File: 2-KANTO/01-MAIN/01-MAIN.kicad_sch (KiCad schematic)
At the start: 69 parts, among them J1 WRITER CONN, J2 Conn_01x05, J3 STS3032, J4 STS3032, J5 STS3032, J6 STS3032, J7 LOADCELL_R, J8 LOADCELL_L, Q1 2SA1015, U1 STM32F446RETx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

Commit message: mike
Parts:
- removed D2, D3, D4, D5, D6, D7, D8, D9: WS2812B, LED_SMD:LED_WS2812B_PLCC4_5.0x5.0mm_P3.2mm, symbol LED:WS2812B
- removed RV1, RV2, RV3: R_Trim, Potentiometer_THT:Potentiometer_Bourns_3296W_Vertical, symbol Device:R_Potentiometer_Trim_US
- added H1: ToMainVDD, MountingHole:MountingHole_3.2mm_M3_Pad_Via, symbol Mechanical:MountingHole_Pad
- added H2: ToMainGND, MountingHole:MountingHole_3.2mm_M3_Pad_Via, symbol Mechanical:MountingHole_Pad
- added J9: MAIN Conn, Connector_JST:JST_XH_B8B-XH-A_1x08_P2.50mm_Vertical, symbol Connector_Generic:Conn_01x08
- added R21, R22: 2.2k, Resistor_SMD:R_0603_1608Metric, symbol Device:R
- added R23: 1.5k, Resistor_SMD:R_0603_1608Metric, symbol Device:R
- J1: footprint Connector_PinSocket_2.54mm:PinSocket_2x04_P2.54mm_Vertical -> Connector_PinSocket_2.54mm:PinSocket_2x04_P2.54mm_Horizontal
- J2: value Conn_01x05 -> toLINE
- J3, J4, J5, J6: footprint Connector_JST:JST_XH_B3B-XH-A_1x03_P2.50mm_Vertical -> Connector_Molex:Molex_SPOX_5267-03A_1x03_P2.50mm_Vertical
- R12, R13, R14, R15: value 330k -> 1M; LCSC C23137 -> C22935
- R16, R17, R18, R19: LCSC C137819 -> C25804
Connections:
- net CK1 is gone; now on net Battery_obs: U1.62 (PB9)
- net Dout1 is gone; now on net I2C1_SDA: U1.59 (PB7)
- net Range1 is gone; now on net I2C2_SCL: U1.29 (PB10)
- net photo_L_6 is gone; now on net LOADCEL_L: U1.9 (PC1)
- net photo_L_7 is gone; now on net LOADCEL_R: U1.8 (PC0)
- net photo_R_1 is gone; now on net XSHUT1: U1.21 (PA5)
- net photo_R_2 is gone; now on net XSHUT2: U1.22 (PA6)
- net photo_R_3 is gone; now on net XSHUT3: U1.23 (PA7)
- net photo_R_7 is gone; now on net buzzer: U1.27 (PB1)
- net +3V3: now also J1.1 (Pin_1), J9.2 (Pin_2); no longer J1.2 (Pin_2)
- net +5V: now also J9.5 (Pin_5)
- net BOOT0: now also J1.4 (Pin_4); no longer J1.3 (Pin_3)
- net GND: now also J1.3 (Pin_3), J3.1 (Pin_1), J4.1 (Pin_1), J5.1 (Pin_1), J6.1 (Pin_1), H2.1, J9.8 (Pin_8), R21.2, R22.2, R23.2; no longer J1.4 (Pin_4), J3.3 (Pin_3), J4.3 (Pin_3), J5.3 (Pin_3), J6.3 (Pin_3)
- net I2C1_SCL: now also U1.58 (PB6)
- net I2C2_SDA: now also U1.55 (PB3)
- net NRST: now also J1.6 (Pin_6); no longer J1.5 (Pin_5)
- net STS_SIG: now also J3.3 (Pin_3), J4.3 (Pin_3), J5.3 (Pin_3), J6.3 (Pin_3); no longer J3.1 (Pin_1), J4.1 (Pin_1), J5.1 (Pin_1), J6.1 (Pin_1)
- net ToF_WS2812B: now also U1.50 (PA15)
- net UART1_RX: now also J1.7 (Pin_7); no longer J1.8 (Pin_8)
- net UART1_TX: now also J1.5 (Pin_5); no longer J1.6 (Pin_6)
- net UART3_RX: no longer J2.3 (Pin_3)
- net UART3_TX: no longer J2.4 (Pin_4)
- net VDD: now also H1.1
- net XSHUT4: now also U1.41 (PA8)
- net XSHUT5: now also U1.45 (PA12)
- net XSHUT6: now also U1.46 (PA13)
- net XSHUT7: now also U1.49 (PA14)
- net MAIN->OpenMV: now reaches U1.37 (PC6)
- net MAIN->OpenMV: now also J9.4 (Pin_4)
- net OpenMV->MAIN: now reaches U1.38 (PC7)
- net OpenMV->MAIN: now also J9.3 (Pin_3)
- net UART5_TX: now reaches U1.53 (PC12)
- net UART5_RX: now reaches U1.54 (PD2)
- net at U3.5 (Trim): now also R21.1
- net at R20.2, U15.2 (IN): now also R23.1
- net at U2.5 (Trim): now also R22.1
- net CK2: no longer names the net of U1.35 (PB14)
- net Dout2: no longer names the net of U1.33 (PB12)
- net Gate1: no longer names the net of U1.61 (PB8)
- net Gate2: no longer names the net of U1.34 (PB13)
- net LED_L: no longer names the net of U1.4 (PC15)
- net LED_R: no longer names the net of U1.3 (PC14)
- net Range2: no longer names the net of U1.36 (PB15)
- net photo_L_1 renamed UART2_TX
- net UART2_TX: now also J2.3 (Pin_3)
- net photo_L_2 renamed PWR->MAIN
- net PWR->MAIN: now also J9.6 (Pin_6)
- net photo_L_3 renamed MAIN->PWR
- net MAIN->PWR: now also J9.7 (Pin_7)
- net photo_L_4: no longer names the net of U1.11 (PC3)
- net photo_L_5: no longer names the net of U1.10 (PC2)
- net photo_R_4: no longer names the net of U1.24 (PC4)
- net photo_R_5: no longer names the net of U1.25 (PC5)
- net photo_R_6: no longer names the net of U1.26 (PB0)
- net photo_center renamed LoPSwitch
- net LoPSwitch: now also J9.1 (Pin_1)
- net photo_front renamed UART2_RX
- net UART2_RX: now also J2.4 (Pin_4)
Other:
- note added: "MAIN F446"
- note added: "UART1:WRITER UART2:LINE UART3:STS3032 UART4:PWR UART5: UART6:OpenMV"
- note removed: "F446RE"
- moved on the sheet: BZ1, D1, J1, J2, R20, R3, U15

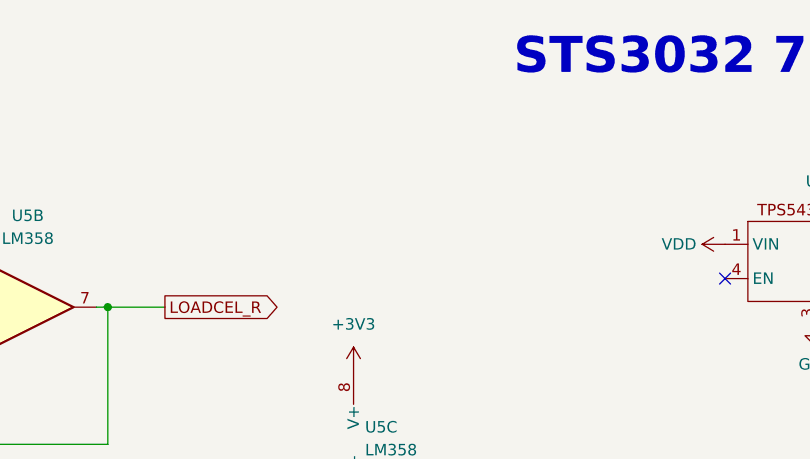
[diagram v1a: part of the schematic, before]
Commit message: 01-MAIN回路図終わり
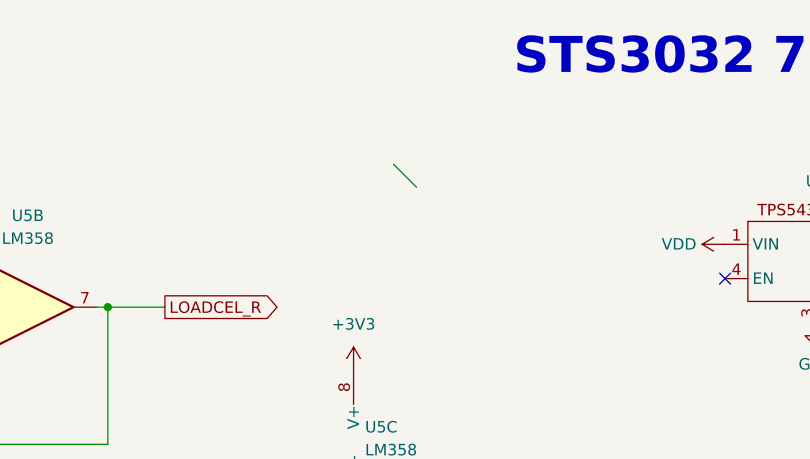
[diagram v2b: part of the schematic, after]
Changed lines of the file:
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@@
   (no_connect (at 73.025 186.055))
   (no_connect (at 95.25 128.27))
+  (bus_entry (at 287.02 38.735) (size 2.54 2.54)
+    (stroke (width 0) (type default))
+  )
   (wire (pts (xy 51.435 69.85) (xy 55.245 69.85))
     (stroke (width 0) (type default))
